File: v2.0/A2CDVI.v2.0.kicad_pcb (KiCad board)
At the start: 2 copper layers, 95 x 51.7 mm, 83 parts, among them U1 Pico, U2 SN74LVC245APWR, U3 SN74LVC245APWR, U4 SN74LVC245APWR, U5 SN74LVC245APWR

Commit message: Initial Layout mess
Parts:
- removed ? (x54): , 
- removed H1: PinHeader_1x01_P2.54mm_Horizontal, Connector_PinHeader_2.54mm:PinHeader_1x01_P2.54mm_Horizontal
- removed R12: 10k, Resistor_SMD:R_0402_1005Metric
- removed U4, U5: SN74LVC245APWR, Package_SO:TSSOP-20_4.4x6.5mm_P0.65mm
- added C8: C, Capacitor_SMD:C_0402_1005Metric_Pad0.74x0.62mm_HandSolder, F.Cu at (61.8, 105.8)
- added C9: C, Capacitor_SMD:C_0402_1005Metric_Pad0.74x0.62mm_HandSolder, F.Cu at (61.8, 107.8)
- added J1: DA15_Plug, Connector_Dsub:DSUB-15_Male_Vertical_P2.77x2.84mm_MountingHoles, F.Cu at (82.2, 150.3)
- added J2: Aux, Connector_PinHeader_1.00mm:PinHeader_2x03_P1.00mm_Vertical, F.Cu at (58.4, 120.8)
- added SW1: Config, Button_Switch_SMD:SW_SPST_PTS645, F.Cu at (51.1, 123.2)
- C7: value C_1210_3225Metric -> 220u; footprint Capacitor_SMD:C_1210_3225Metric -> Capacitor_SMD:C_1210_3225Metric_Pad1.33x2.70mm_HandSolder
- D1: value SS16 -> MBR120VLSFT1G; footprint Diode_SMD:D_SMA -> Diode_THT:D_DO-35_SOD27_P7.62mm_Horizontal
- Fu1: value Fuse_0805_2012Metric -> Polyfuse 100mA; footprint Fuse:Fuse_0805_2012Metric -> Fuse:Fuse_0805_2012Metric_Pad1.15x1.40mm_HandSolder
- HDMI1: value HDMI_A_Molex_208658-1001_Horizontal -> HDMI-SWM-19; footprint Connector_HDMI:HDMI_A_Molex_208658-1001_Horizontal -> Connector_Video:HDMI_A_Molex_208658-1001_Horizontal
- R10: value 10k -> 10K
- R11: value 10k -> 1k
- U1: value Pico -> RPI-Pico; footprint RaspberryPI PicoW:RPi_PicoW_SMD_TH -> MCU_RaspberryPi_and_Boards:RPi_Pico_SMD_TH
- U2: value SN74LVC245APWR -> L7805; footprint Package_SO:TSSOP-20_4.4x6.5mm_P0.65mm -> Package_TO_SOT_SMD:TO-252-2
- U3: value SN74LVC245APWR -> 74LVC245
- moved D1 128.7 mm to (47.1, 128.9), turned to 0 degrees
- moved C5 109.9 mm to (61.8, 101.9)
- moved C4 100.1 mm to (61.8, 99.9)
- moved C3 90.7 mm to (61.8, 98.0)
- moved R11 89.7 mm to (67.6, 124.2)
- moved C6 85.3 mm to (61.8, 103.9)
- moved C2 81.6 mm to (61.8, 96.0)
- moved U2 79.0 mm to (52.5, 115.2), turned to 0 degrees
- moved R10 65.4 mm to (81.0, 129.0), turned to -90 degrees
- moved U3 64.6 mm to (76.6, 124.8)
- moved R9 54.7 mm to (81.0, 131.2), turned to -90 degrees
- moved C7 49.4 mm to (139.2, 154.7), turned to 0 degrees
- moved C1 42.2 mm to (61.8, 94.0)
- moved Fu1 33.8 mm to (151.8, 155.4), turned to 0 degrees
- moved R7 0.19 mm to (142.1, 108.1)
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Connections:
- net CK_N renamed Net-(U1-GP15)
- net CK_P renamed Net-(U1-GP14)
- net D0_N renamed Net-(U1-GP21)
- net D0_P renamed Net-(U1-GP20)
- net D1_N renamed Net-(U1-GP19)
- net D1_P renamed Net-(U1-GP18)
- net D2_N renamed Net-(U1-GP17)
- net D2_P renamed Net-(U1-GP16)
- net D2_otut_P renamed /D2+
- C1 pad 1: VSYS -> +3V3
- C2 pad 1: 3.3V -> +3V3
- C3 pad 1: 3.3V -> +3V3
- C4 pad 1: 3.3V -> +3V3
- C5 pad 1: 3.3V -> +3V3
- C6 pad 1: 5V_out -> Net-(C6-Pad1)
- C7 pad 1: GND -> +5V
- C7 pad 2: 5V -> GND
- D1 pad 1: VSYS -> Net-(D1-K)
- D1 pad 2: 5V -> +5V
- Fu1 pad 1: 5V_out -> Net-(D1-K)
- Fu1 pad 2: 5V -> Net-(C6-Pad1)
- HDMI1 pad 10: (no net) -> /CK+
- HDMI1 pad 12: (no net) -> /CK-
- HDMI1 pad 13: (no net) -> unconnected-(HDMI1-Pad13)
- HDMI1 pad 14: (no net) -> unconnected-(HDMI1-Pad14)
- HDMI1 pad 15: (no net) -> unconnected-(HDMI1-Pad15)
- HDMI1 pad 16: (no net) -> unconnected-(HDMI1-Pad16)
- HDMI1 pad 18: 5V_out -> Net-(C6-Pad1)
- HDMI1 pad 19: (no net) -> unconnected-(HDMI1-Pad19)
- HDMI1 pad 3: (no net) -> /D2-
- HDMI1 pad 4: (no net) -> /D1+
- HDMI1 pad 6: (no net) -> /D1-
- HDMI1 pad 7: (no net) -> /D0+
- HDMI1 pad 9: (no net) -> /D0-
- HDMI1 pad SH: GND -> (no net)
- R10 pad 1: DATAOE -> +3V3
- R10 pad 2: 3.3V -> Net-(U1-GP11)
- R11 pad 1: MSBOE -> Net-(J2-Pin_6)
- R11 pad 2: 3.3V -> +5V
- R2 pad 2: (no net) -> /D2-
- R3 pad 2: (no net) -> /D1+
- R4 pad 2: (no net) -> /D1-
- R5 pad 2: (no net) -> /D0+
- R6 pad 2: (no net) -> /D0-
- R7 pad 2: (no net) -> /CK+
- R8 pad 2: (no net) -> /CK-
- R9 pad 1: LSBOE -> Net-(U3-B0)
- R9 pad 2: 3.3V -> GND
- U1 pad 1: AD0 -> unconnected-(U1-GP0-Pad1)
- U1 pad 10: AD7 -> unconnected-(U1-GP7-Pad10)
- U1 pad 11: L-DevSel -> unconnected-(U1-GP8-Pad11)
- U1 pad 12: L-RW -> unconnected-(U1-GP9-Pad12)
- U1 pad 14: GP10 -> unconnected-(U1-GP10-Pad14)
- U1 pad 15: DATAOE -> Net-(U1-GP11)
- U1 pad 16: LSBOE -> unconnected-(U1-GP12-Pad16)
- U1 pad 17: MSBOE -> unconnected-(U1-GP13-Pad17)
- U1 pad 2: AD1 -> unconnected-(U1-GP1-Pad2)
- U1 pad 29: (no net) -> unconnected-(U1-GP22-Pad29)
- U1 pad 30: (no net) -> unconnected-(U1-RUN-Pad30)
- U1 pad 31: L-PHI0 -> unconnected-(U1-GP26-Pad31)
- U1 pad 32: (no net) -> unconnected-(U1-GP27-Pad32)
- U1 pad 34: (no net) -> unconnected-(U1-GP28-Pad34)
- U1 pad 35: (no net) -> unconnected-(U1-ADC_VREF-Pad35)
- U1 pad 36: 3.3V -> +3V3
- U1 pad 37: (no net) -> unconnected-(U1-3V3_EN-Pad37)
- U1 pad 39: VSYS -> Net-(D1-K)
- U1 pad 4: AD2 -> unconnected-(U1-GP2-Pad4)
- U1 pad 40: (no net) -> unconnected-(U1-VBUS-Pad40)
- U1 pad 5: AD3 -> unconnected-(U1-GP3-Pad5)
- U1 pad 6: AD4 -> unconnected-(U1-GP4-Pad6)
- U1 pad 7: AD5 -> unconnected-(U1-GP5-Pad7)
- U1 pad 9: AD6 -> unconnected-(U1-GP6-Pad9)
- U2 pad 1: GND -> +12V
- U2 pad 2: AD7 -> GND
- U2 pad 3: AD6 -> +5V
- U3 pad 11: D0 -> Net-(J1-SEROUT)
- U3 pad 12: D1 -> Net-(J1-14M)
- U3 pad 13: D2 -> Net-(J1-WNDW)
- U3 pad 14: D3 -> Net-(J1-TEXT)
- U3 pad 15: D4 -> Net-(J1-GR)
- U3 pad 16: D5 -> Net-(J2-Pin_1)
- U3 pad 17: D6 -> Net-(J2-Pin_3)
- U3 pad 18: D7 -> Net-(U3-B0)
- U3 pad 19: DATAOE -> Net-(U1-GP11)
- U3 pad 2: AD7 -> unconnected-(U3-A0-Pad2)
- U3 pad 20: 3.3V -> +3V3
- U3 pad 3: AD6 -> unconnected-(U3-A1-Pad3)
- U3 pad 4: AD5 -> unconnected-(U3-A2-Pad4)
- U3 pad 5: AD4 -> unconnected-(U3-A3-Pad5)
- U3 pad 6: AD3 -> unconnected-(U3-A4-Pad6)
- U3 pad 7: AD2 -> unconnected-(U3-A5-Pad7)
- U3 pad 8: AD1 -> unconnected-(U3-A6-Pad8)
- U3 pad 9: AD0 -> unconnected-(U3-A7-Pad9)
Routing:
- net (no net): track 39.2 -> 619.8 mm, vias 2 -> 17
- net VSYS: track 141.0 -> 0.00 mm, vias 4 -> 0
- net Net-(D1-K): track 0.00 -> 141.0 mm, vias 0 -> 4
- net 3.3V: track 136.7 -> 0.00 mm, vias 6 -> 0
- net +3V3: track 0.00 -> 136.7 mm, vias 0 -> 6
- net unconnected-(U1-GP26-Pad31): track 0.00 -> 73.9 mm, vias 0 -> 2
- net L-PHI0: track 73.9 -> 0.00 mm, vias 2 -> 0
- net unconnected-(U1-GP0-Pad1): track 0.00 -> 73.3 mm, vias 0 -> 4
- net AD0: track 73.3 -> 0.00 mm, vias 4 -> 0
- net unconnected-(U1-GP1-Pad2): track 0.00 -> 70.7 mm, vias 0 -> 4
- net AD1: track 70.7 -> 0.00 mm, vias 4 -> 0
- net unconnected-(U1-GP7-Pad10): track 0.00 -> 69.5 mm, vias 0 -> 4
- net AD7: track 69.5 -> 0.00 mm, vias 4 -> 0
- net unconnected-(U1-GP5-Pad7): track 0.00 -> 68.7 mm, vias 0 -> 4
- net AD5: track 68.7 -> 0.00 mm, vias 4 -> 0
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
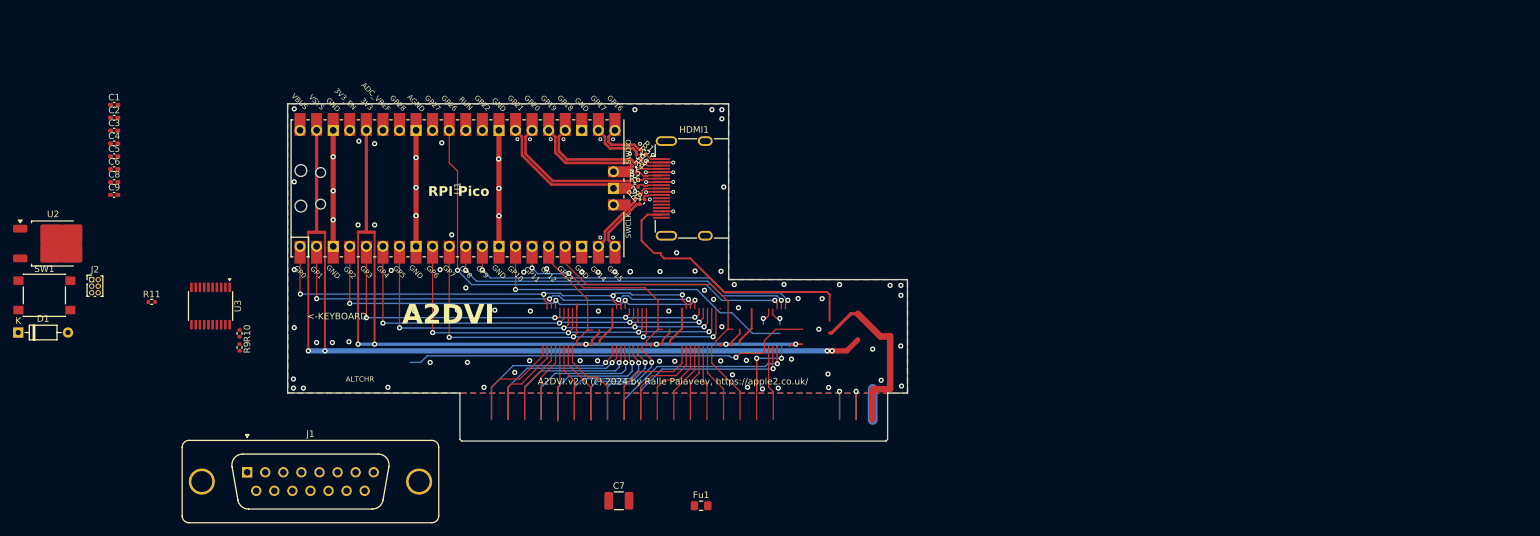
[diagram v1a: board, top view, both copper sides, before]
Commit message: Basic Board Layout
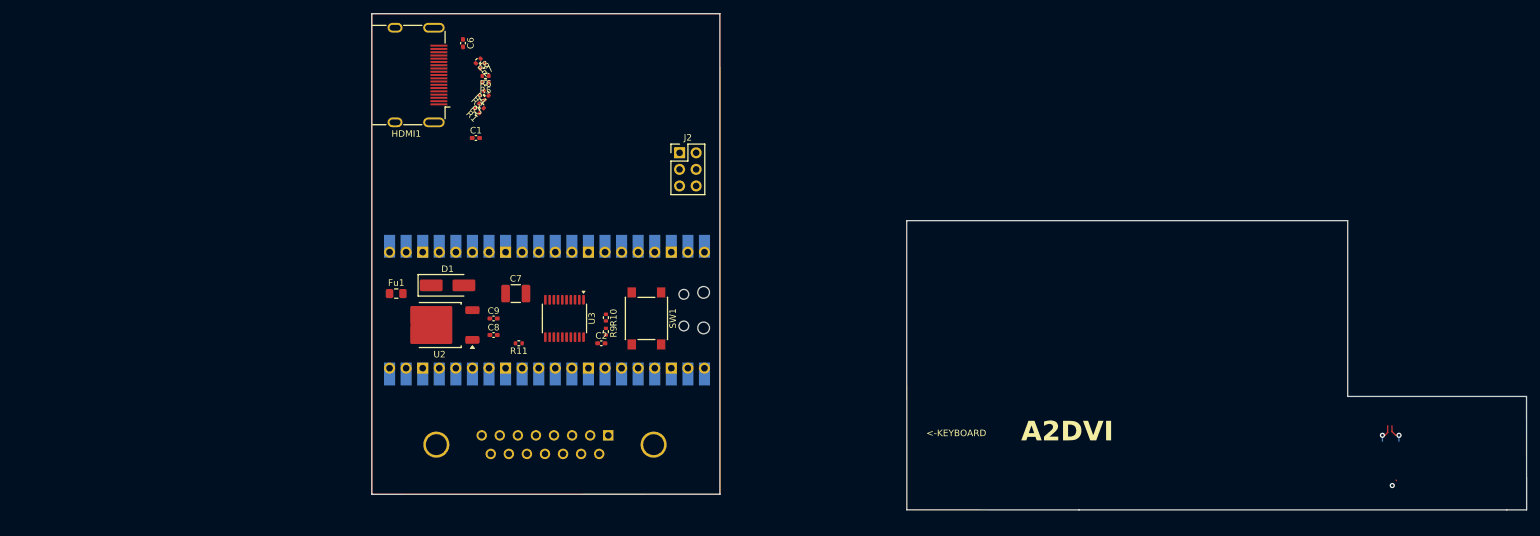
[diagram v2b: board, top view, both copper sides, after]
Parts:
- removed C3, C4, C5: 100n, Capacitor_SMD:C_0402_1005Metric_Pad0.74x0.62mm_HandSolder
- D1: footprint Diode_THT:D_DO-35_SOD27_P7.62mm_Horizontal -> Diode_SMD:D_SMA_Handsoldering
- J1: moved to B.Cu
- J2: footprint Connector_PinHeader_1.00mm:PinHeader_2x03_P1.00mm_Vertical -> Connector_PinHeader_2.54mm:PinHeader_2x03_P2.54mm_Vertical
- U1: footprint MCU_RaspberryPi_and_Boards:RPi_Pico_SMD_TH -> MCU_RaspberryPi_and_Boards:RPi_Pico_SMD_TH_NO_DEBUG; moved to B.Cu
- moved REF** 96.5 mm to (272.3, 152.9)
- moved SW1 92.3 mm to (143.4, 126.7), turned to -90 degrees
- moved J2 92.2 mm to (148.5, 101.3)
- moved C2 82.3 mm to (136.5, 130.5)
- moved D1 66.2 mm to (112.9, 121.7)
- moved C8 62.7 mm to (120.0, 129.3)
- moved C9 61.1 mm to (120.0, 126.7)
- moved U2 60.5 mm to (111.7, 127.7), turned to 180 degrees
- moved Fu1 56.9 mm to (105.0, 122.9)
- moved C6 56.8 mm to (115.3, 84.5), turned to -90 degrees
- moved R11 56.6 mm to (123.8, 130.5), turned to 180 degrees
- moved R10 56.2 mm to (137.2, 126.6)
- moved R9 56.2 mm to (137.2, 128.8)
- moved C1 55.7 mm to (117.2, 99.1)
- moved J1 55.6 mm to (137.5, 144.7), turned to 180 degrees
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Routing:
- net (no net): track 619.8 -> 6.29 mm, vias 17 -> 3
- net Net-(D1-K): track 141.0 -> 0.00 mm, vias 4 -> 0
- net +3V3: track 136.7 -> 0.00 mm, vias 6 -> 0
- net GND: track 96.0 -> 0.00 mm, vias 109 -> 0
- net unconnected-(U1-GP26-Pad31): track 73.9 -> 0.00 mm, vias 2 -> 0
- net unconnected-(U1-GP0-Pad1): track 73.3 -> 0.00 mm, vias 4 -> 0
- net unconnected-(U1-GP1-Pad2): track 70.7 -> 0.00 mm, vias 4 -> 0
- net unconnected-(U1-GP7-Pad10): track 69.5 -> 0.00 mm, vias 4 -> 0
- net unconnected-(U1-GP5-Pad7): track 68.7 -> 0.00 mm, vias 4 -> 0
- net unconnected-(U1-GP4-Pad6): track 67.6 -> 0.00 mm, vias 4 -> 0
- net unconnected-(U1-GP6-Pad9): track 67.3 -> 0.00 mm, vias 4 -> 0
- net unconnected-(U1-GP3-Pad5): track 67.1 -> 0.00 mm, vias 4 -> 0
- net unconnected-(U1-GP2-Pad4): track 67.1 -> 0.00 mm, vias 4 -> 0
- net unconnected-(U1-GP8-Pad11): track 55.3 -> 0.00 mm, vias 2 -> 0
- net unconnected-(U1-GP9-Pad12): track 53.8 -> 0.00 mm, vias 2 -> 0
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- removed copper zone on B.Cu, net GND
- removed copper zone on F.Cu, net GND
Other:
- board size 95 x 51.7 mm -> 177 x 76 mm
- board text added: "<-- USB Here"
- board text removed: "A2DVI.v2.0 (c) 2024 by Ralle Palaveev, https://apple2.co.uk/"
- board text removed: "ALTCHR"

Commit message: Tracks drawn
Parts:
- moved REF** 122.6 mm to (149.7, 149.6)
- moved R11 38.1 mm to (152.3, 105.1), turned to -90 degrees
- moved C9 33.9 mm to (149.2, 109.6), turned to 180 degrees
- moved SW1 30.1 mm to (147.2, 96.9), turned to 180 degrees
- moved C1 28.6 mm to (142.7, 112.1)
- moved HDMI1 21.6 mm to (126.5, 101.0)
- moved C6 21.6 mm to (133.5, 96.1)
- moved R4 20.8 mm to (134.5, 105.9), turned to -90 degrees
- moved R8 20.7 mm to (134.8, 98.8), turned to 180 degrees
- moved R5 20.6 mm to (135.1, 103.0)
- moved R6 20.6 mm to (135.1, 102.0)
- moved R7 20.4 mm to (134.8, 99.9), turned to 180 degrees
- moved C7 20.1 mm to (143.4, 121.7)
- moved R3 19.9 mm to (133.2, 105.9), turned to 90 degrees
- moved R1 17.3 mm to (122.5, 111.4), turned to 180 degrees
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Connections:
- Fu1 pad 1: Net-(D1-K) -> Net-(J1-+12V)
- Fu1 pad 2: Net-(C6-Pad1) -> +12V
- J1 pad 0: (no net) -> GND
- J1 pad 8: +12V -> Net-(J1-+12V)
- R1 pad 1: Net-(U1-GP16) -> /D2+
- R2 pad 1: Net-(U1-GP17) -> /D2-
- R3 pad 1: Net-(U1-GP18) -> /D1+
- R4 pad 1: Net-(U1-GP19) -> /D1-
- R5 pad 1: Net-(U1-GP20) -> /D0+
- R6 pad 1: Net-(U1-GP21) -> /D0-
- R7 pad 1: Net-(U1-GP14) -> /CK+
- R8 pad 1: Net-(U1-GP15) -> /CK-
- U1 pad 19: Net-(U1-GP14) -> /CK+
- U1 pad 20: Net-(U1-GP15) -> /CK-
- U1 pad 21: Net-(U1-GP16) -> /D2+
- U1 pad 22: Net-(U1-GP17) -> /D2-
- U1 pad 24: Net-(U1-GP18) -> /D1+
- U1 pad 25: Net-(U1-GP19) -> /D1-
- U1 pad 26: Net-(U1-GP20) -> /D0+
- U1 pad 27: Net-(U1-GP21) -> /D0-
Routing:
- net GND: track 0.00 -> 158.7 mm
- net /CK-: track 0.00 -> 62.5 mm, vias 0 -> 2
- net /CK+: track 0.00 -> 58.3 mm, vias 0 -> 2
- net +5V: track 0.00 -> 58.2 mm, vias 0 -> 2
- net Net-(U3-B0): track 0.00 -> 46.8 mm
- net Net-(J2-Pin_3): track 0.00 -> 37.4 mm, vias 0 -> 1
- net /D2-: track 0.00 -> 34.7 mm, vias 0 -> 1
- net /D0+: track 0.00 -> 34.2 mm, vias 0 -> 1
- net /D0-: track 0.00 -> 33.7 mm, vias 0 -> 1
- net /D2+: track 0.00 -> 33.5 mm, vias 0 -> 1
- net Net-(J2-Pin_1): track 0.00 -> 33.1 mm, vias 0 -> 1
- net /D1+: track 0.00 -> 32.0 mm, vias 0 -> 1
- net /D1-: track 0.00 -> 31.6 mm, vias 0 -> 1
- net Net-(D1-K): track 0.00 -> 28.8 mm, vias 0 -> 1
- net +3V3: track 0.00 -> 24.1 mm
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- added copper zone on B.Cu, net GND
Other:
- board size 177 x 76 mm -> 53.4 x 62.5 mm
- board text removed: "<-KEYBOARD"
- board text removed: "A2DVI"
- board text removed: "KEYBOARD->"
- board text removed: "sync altchr"

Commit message: Ready for v1
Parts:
- added REF**: MountingHole_2.5mm_Pad, MountingHole:MountingHole_2.5mm_Pad, F.Cu at (105.3, 150.2)
- added REF**: MountingHole_2.5mm_Pad, MountingHole:MountingHole_2.5mm_Pad, F.Cu at (137.0, 95.6)
- added REF**: MountingHole_2.5mm_Pad, MountingHole:MountingHole_2.5mm_Pad, F.Cu at (151.0, 150.2)
- moved REF** 48.8 mm to (109.7, 121.7)
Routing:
- net GND: track 158.7 -> 161.3 mm, vias 0 -> 35
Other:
- board text added: "A2CDVI.v1.0 Board design by Josh Clark, (c) 2025 Firmware by Mike Neil, (c) 2025"
- board text removed: "A2DVI.v2.0 Board design by R. Palaveev, (c) 2024 Firmware by Thorsten Brehm, (c) 2024"

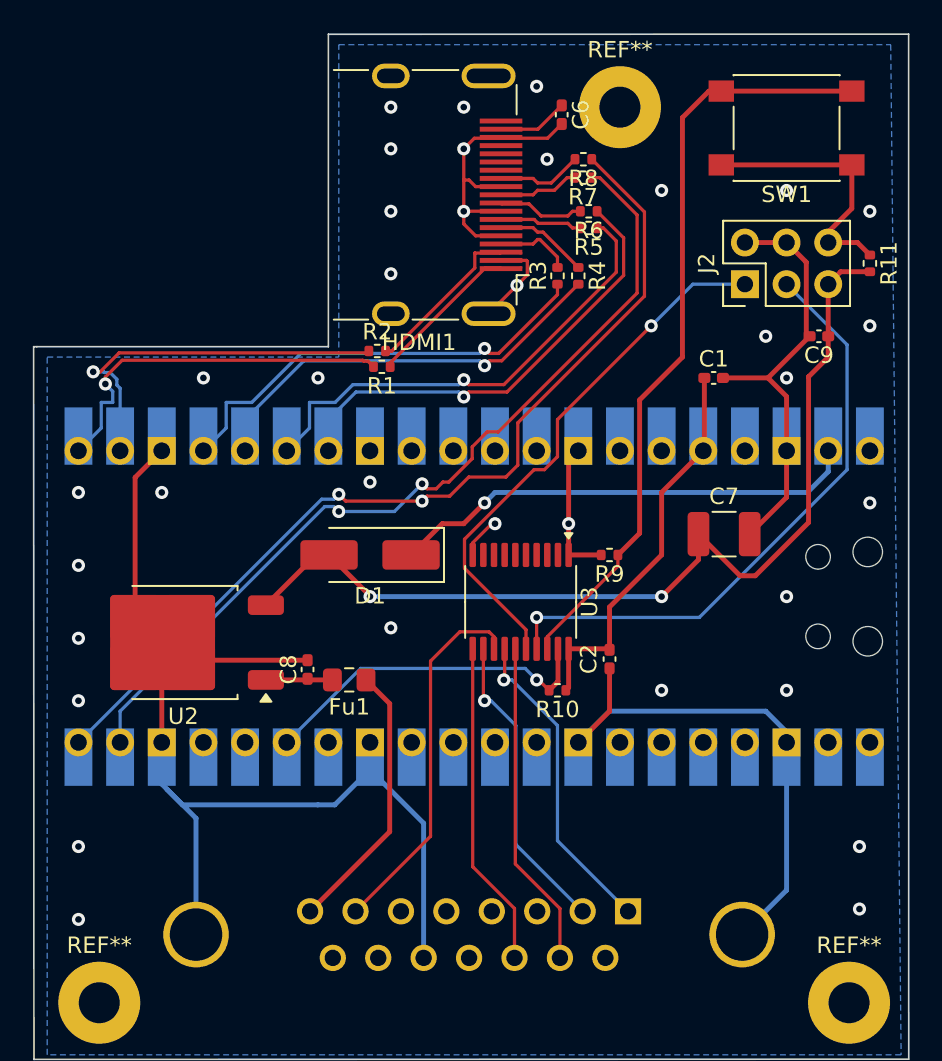
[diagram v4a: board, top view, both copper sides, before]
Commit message: Fixed missing connections in schematic
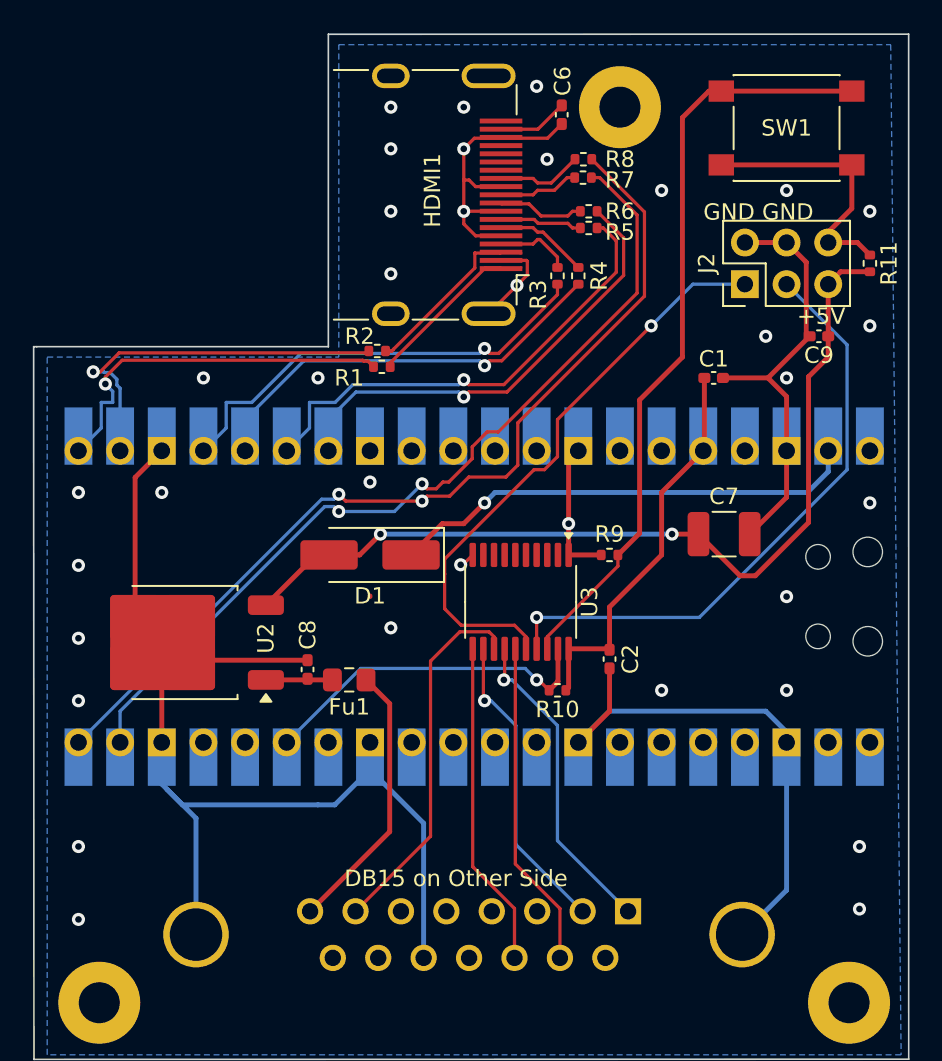
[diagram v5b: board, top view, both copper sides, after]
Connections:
- J1 pad 0: GND -> (no net)
- U1 pad 1: unconnected-(U1-GP0-Pad1) -> Net-(U1-GP0)
- U1 pad 10: unconnected-(U1-GP7-Pad10) -> Net-(U1-GP7)
- U1 pad 2: unconnected-(U1-GP1-Pad2) -> Net-(U1-GP1)
- U1 pad 4: unconnected-(U1-GP2-Pad4) -> Net-(U1-GP2)
- U1 pad 5: unconnected-(U1-GP3-Pad5) -> Net-(U1-GP3)
- U1 pad 6: unconnected-(U1-GP4-Pad6) -> Net-(U1-GP4)
- U1 pad 7: unconnected-(U1-GP5-Pad7) -> Net-(U1-GP5)
- U1 pad 9: unconnected-(U1-GP6-Pad9) -> Net-(U1-GP6)
- U3 pad 2: unconnected-(U3-A0-Pad2) -> Net-(U1-GP7)
- U3 pad 3: unconnected-(U3-A1-Pad3) -> Net-(U1-GP6)
- U3 pad 4: unconnected-(U3-A2-Pad4) -> Net-(U1-GP5)
- U3 pad 5: unconnected-(U3-A3-Pad5) -> Net-(U1-GP4)
- U3 pad 6: unconnected-(U3-A4-Pad6) -> Net-(U1-GP3)
- U3 pad 7: unconnected-(U3-A5-Pad7) -> Net-(U1-GP2)
- U3 pad 8: unconnected-(U3-A6-Pad8) -> Net-(U1-GP1)
- U3 pad 9: unconnected-(U3-A7-Pad9) -> Net-(U1-GP0)
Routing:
- net +5V: track 58.2 -> 55.2 mm
- net Net-(J2-Pin_1): track 33.1 -> 36.0 mm
- net GND: track 161.3 -> 159.7 mm
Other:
- board text added: "+5V"
- board text added: "DB15 on Other Side"
- board text added: "GND GND"
- board text added: "RPI Pico On this side"
- board text removed: "RPI Pico"
